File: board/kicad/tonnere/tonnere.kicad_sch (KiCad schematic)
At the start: 10 parts

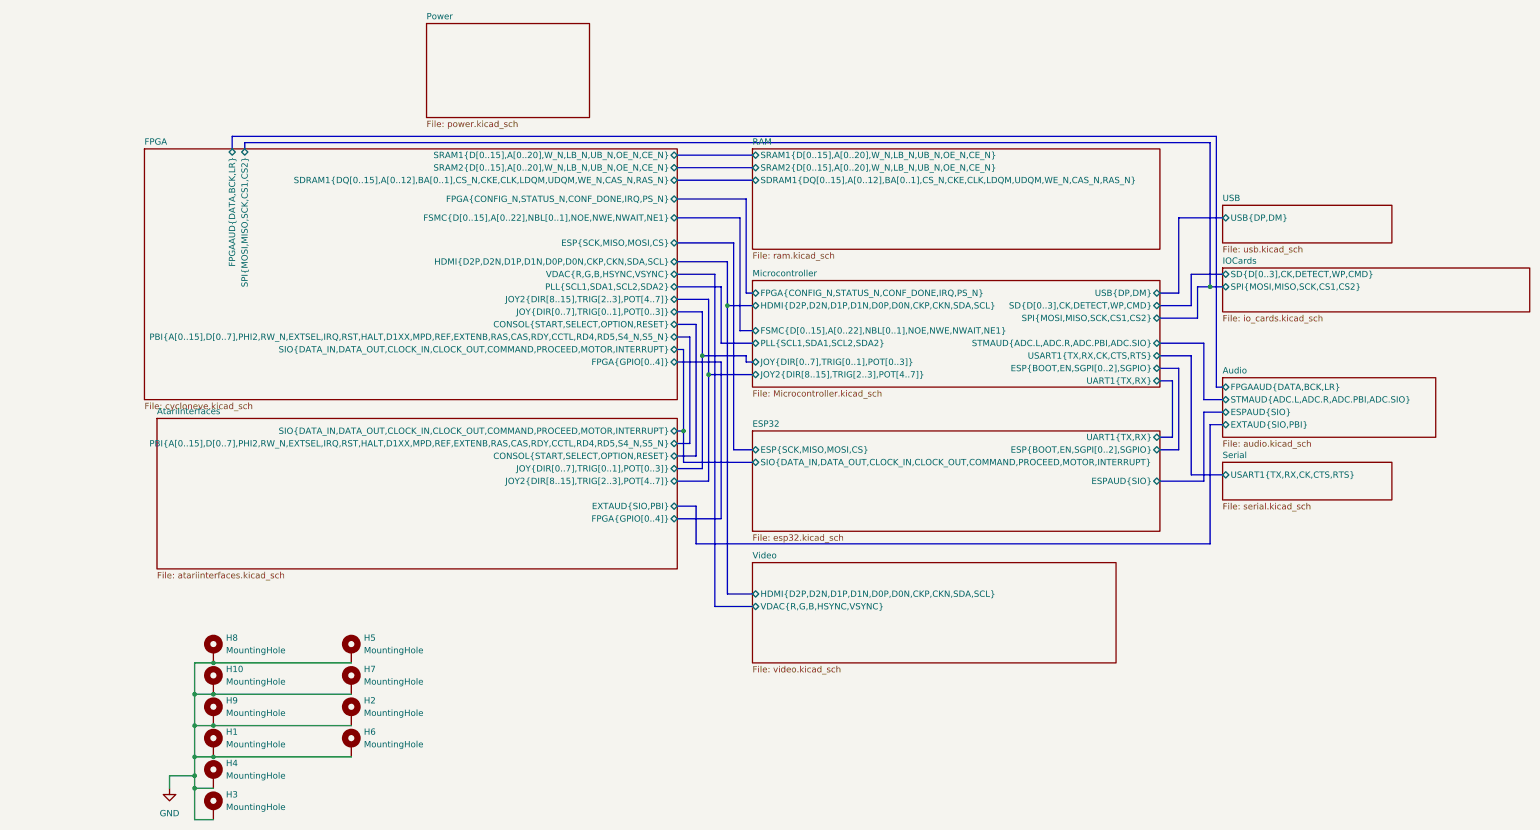
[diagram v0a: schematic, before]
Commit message: 0.60 (not final). Fix errata from 0.51. Added USB2 phy.
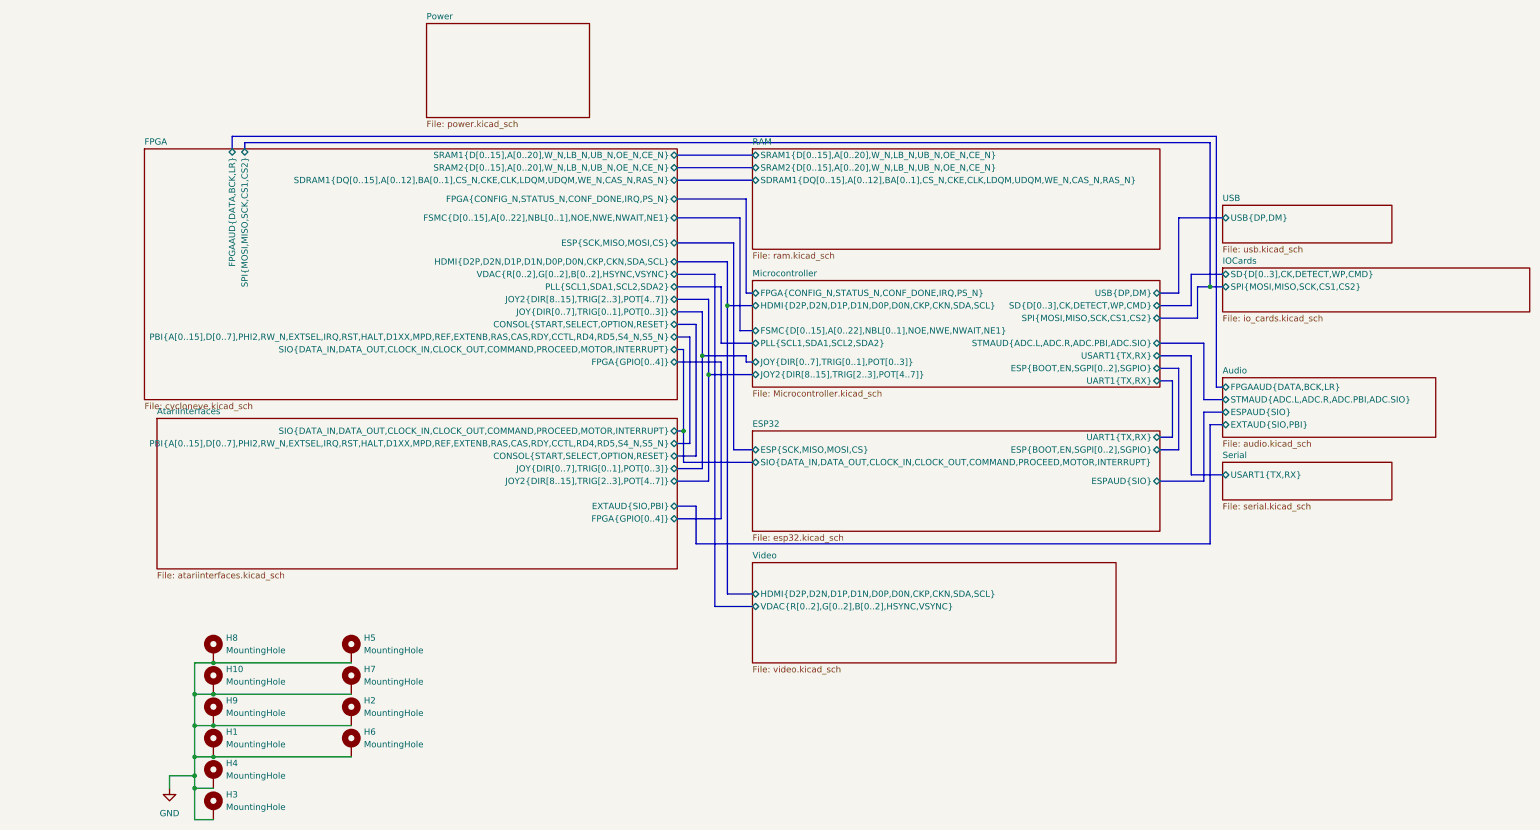
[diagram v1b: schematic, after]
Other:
- sheet FPGA ports: added VDAC{R[0..2],G[0..2],B[0..2],HSYNC,VSYNC}; removed VDAC{R,G,B,HSYNC,VSYNC}
- sheet Microcontroller ports: added USART1{TX,RX}; removed USART1{TX,RX,CK,CTS,RTS}
- sheet Serial ports: added USART1{TX,RX}; removed USART1{TX,RX,CK,CTS,RTS}
- sheet Video ports: added VDAC{R[0..2],G[0..2],B[0..2],HSYNC,VSYNC}; removed VDAC{R,G,B,HSYNC,VSYNC}
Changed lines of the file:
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@@
 			)
 		)
-		(pin "VDAC{R,G,B,HSYNC,VSYNC}" bidirectional
+		(pin "VDAC{R[0..2],G[0..2],B[0..2],HSYNC,VSYNC}" bidirectional
 			(at 134.62 152.4 180)
 			(effects
@@
 			)
 		)
-		(pin "VDAC{R,G,B,HSYNC,VSYNC}" bidirectional
-			(at 119.38 85.09 0)
-			(effects
-				(font
-					(size 1.27 1.27)
-				)
-				(justify right)
-			)
-		)
 		(pin "FPGAAUD{DATA,BCK,LR}" bidirectional
 			(at 29.21 59.69 90)
@@
 		(pin "FPGA{CONFIG_N,STATUS_N,CONF_DONE,IRQ,PS_N}" bidirectional
 			(at 119.38 69.85 0)
+			(effects
+				(font
+					(size 1.27 1.27)
+				)
+				(justify right)
+			)
+		)
+		(pin "VDAC{R[0..2],G[0..2],B[0..2],HSYNC,VSYNC}" bidirectional
+			(at 119.38 85.09 0)
 			(effects
 				(font
@@
 			)
 		)
-		(pin "USART1{TX,RX,CK,CTS,RTS}" bidirectional
-			(at 217.17 101.6 0)
-			(effects
-				(font
-					(size 1.27 1.27)
-				)
-				(justify right)
-			)
-		)
 		(pin "FSMC{D[0..15],A[0..22],NBL[0..1],NOE,NWE,NWAIT,NE1}" bidirectional
 			(at 134.62 96.52 180)
@@
 		(pin "ESP{BOOT,EN,SGPI[0..2],SGPIO}" bidirectional
 			(at 217.17 104.14 0)
+			(effects
+				(font
+					(size 1.27 1.27)
+				)
+				(justify right)
+			)
+		)
+		(pin "USART1{TX,RX}" bidirectional
+			(at 217.17 101.6 0)
 			(effects
 				(font
@@
 			)
 		)
-		(pin "USART1{TX,RX,CK,CTS,RTS}" bidirectional
+		(pin "USART1{TX,RX}" bidirectional
 			(at 229.87 125.73 180)
 			(effects
